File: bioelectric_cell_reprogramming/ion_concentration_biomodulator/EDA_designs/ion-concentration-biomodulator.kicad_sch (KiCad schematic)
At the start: 52 parts, among them J1 532610671, J10 39-53-2045, J11 Conn_01x14_Pin, J12 Conn_01x14_Pin, J13 39-53-2045, J14 39-53-2045, J15 Conn_ARM_SWD_TagConnect_TC2030, J16 IPL1-104-01-L-D-K, J17 Conn_01x02_Pin, J18 EJ508A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

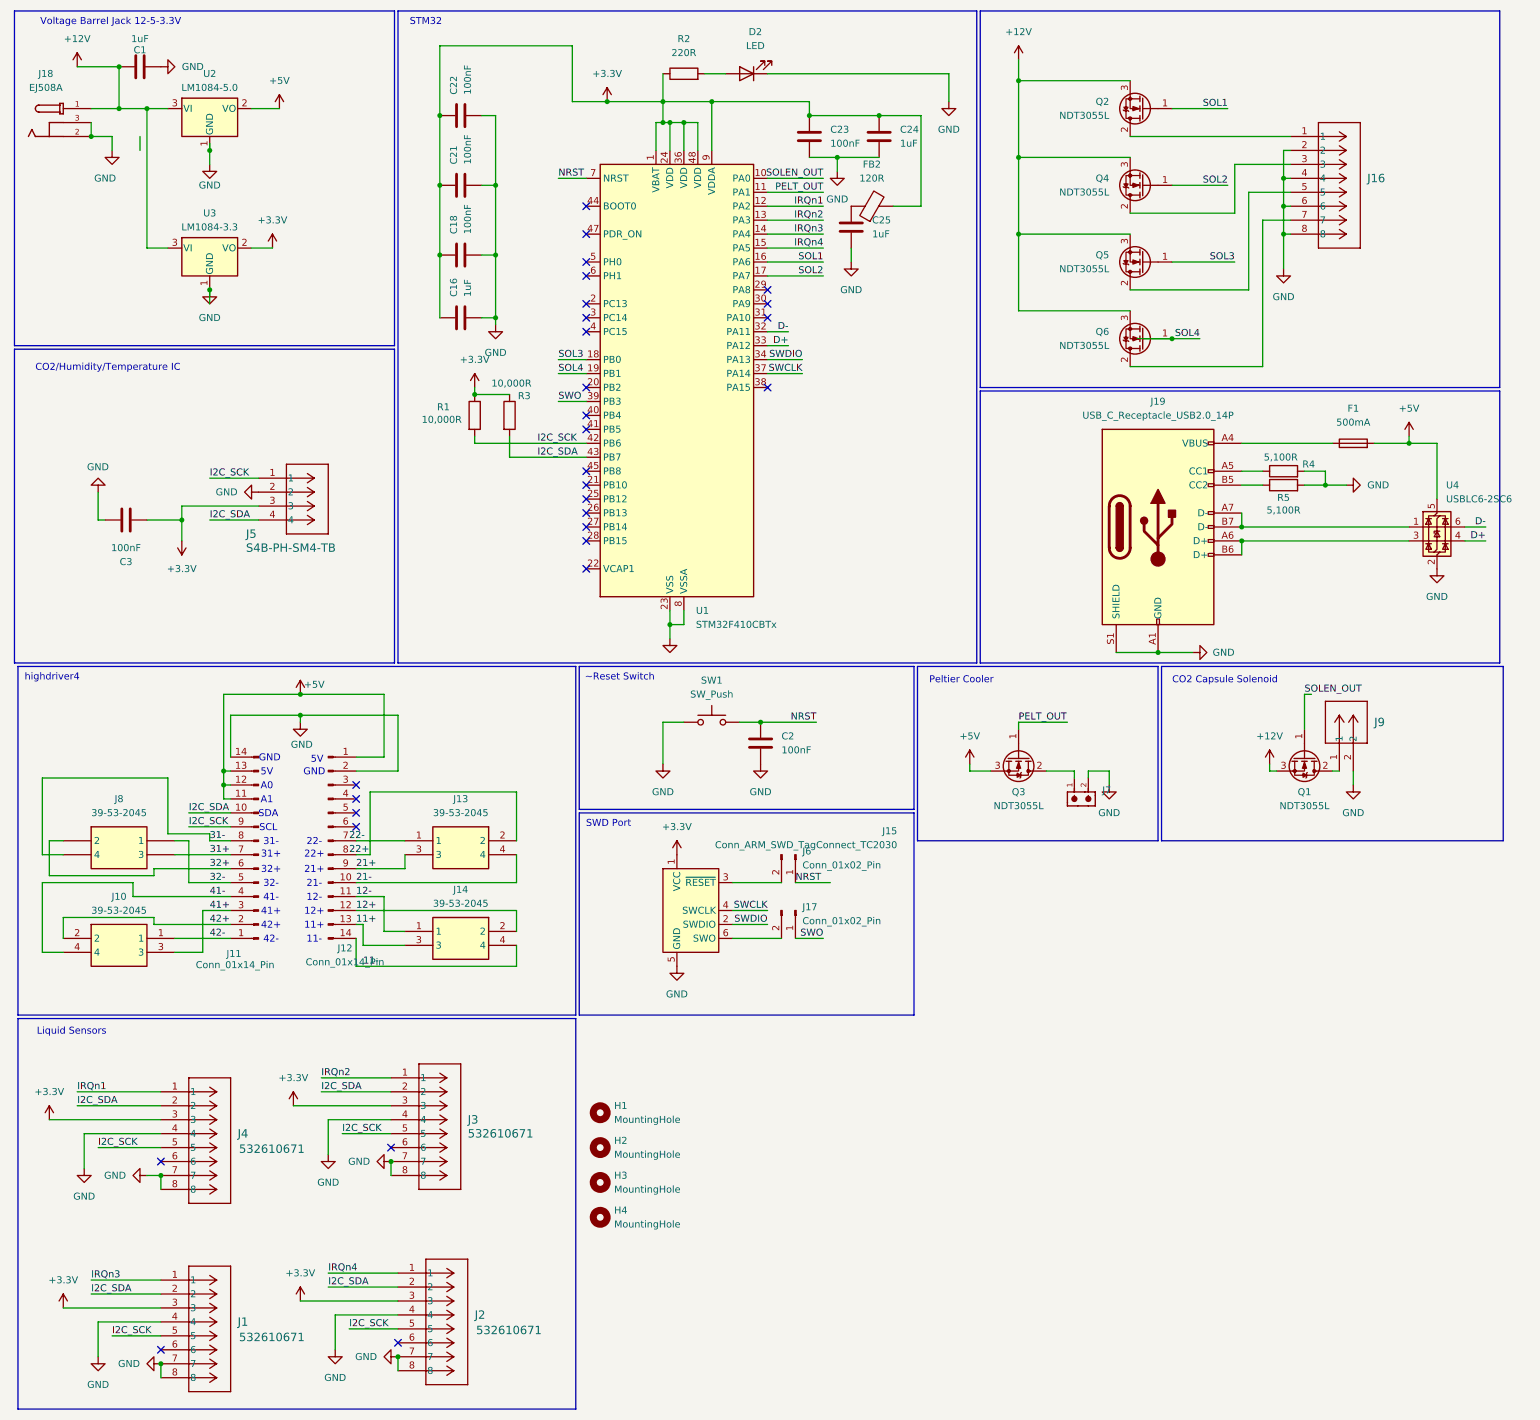
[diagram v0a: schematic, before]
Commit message: Pushed net changes to v7 ICBM
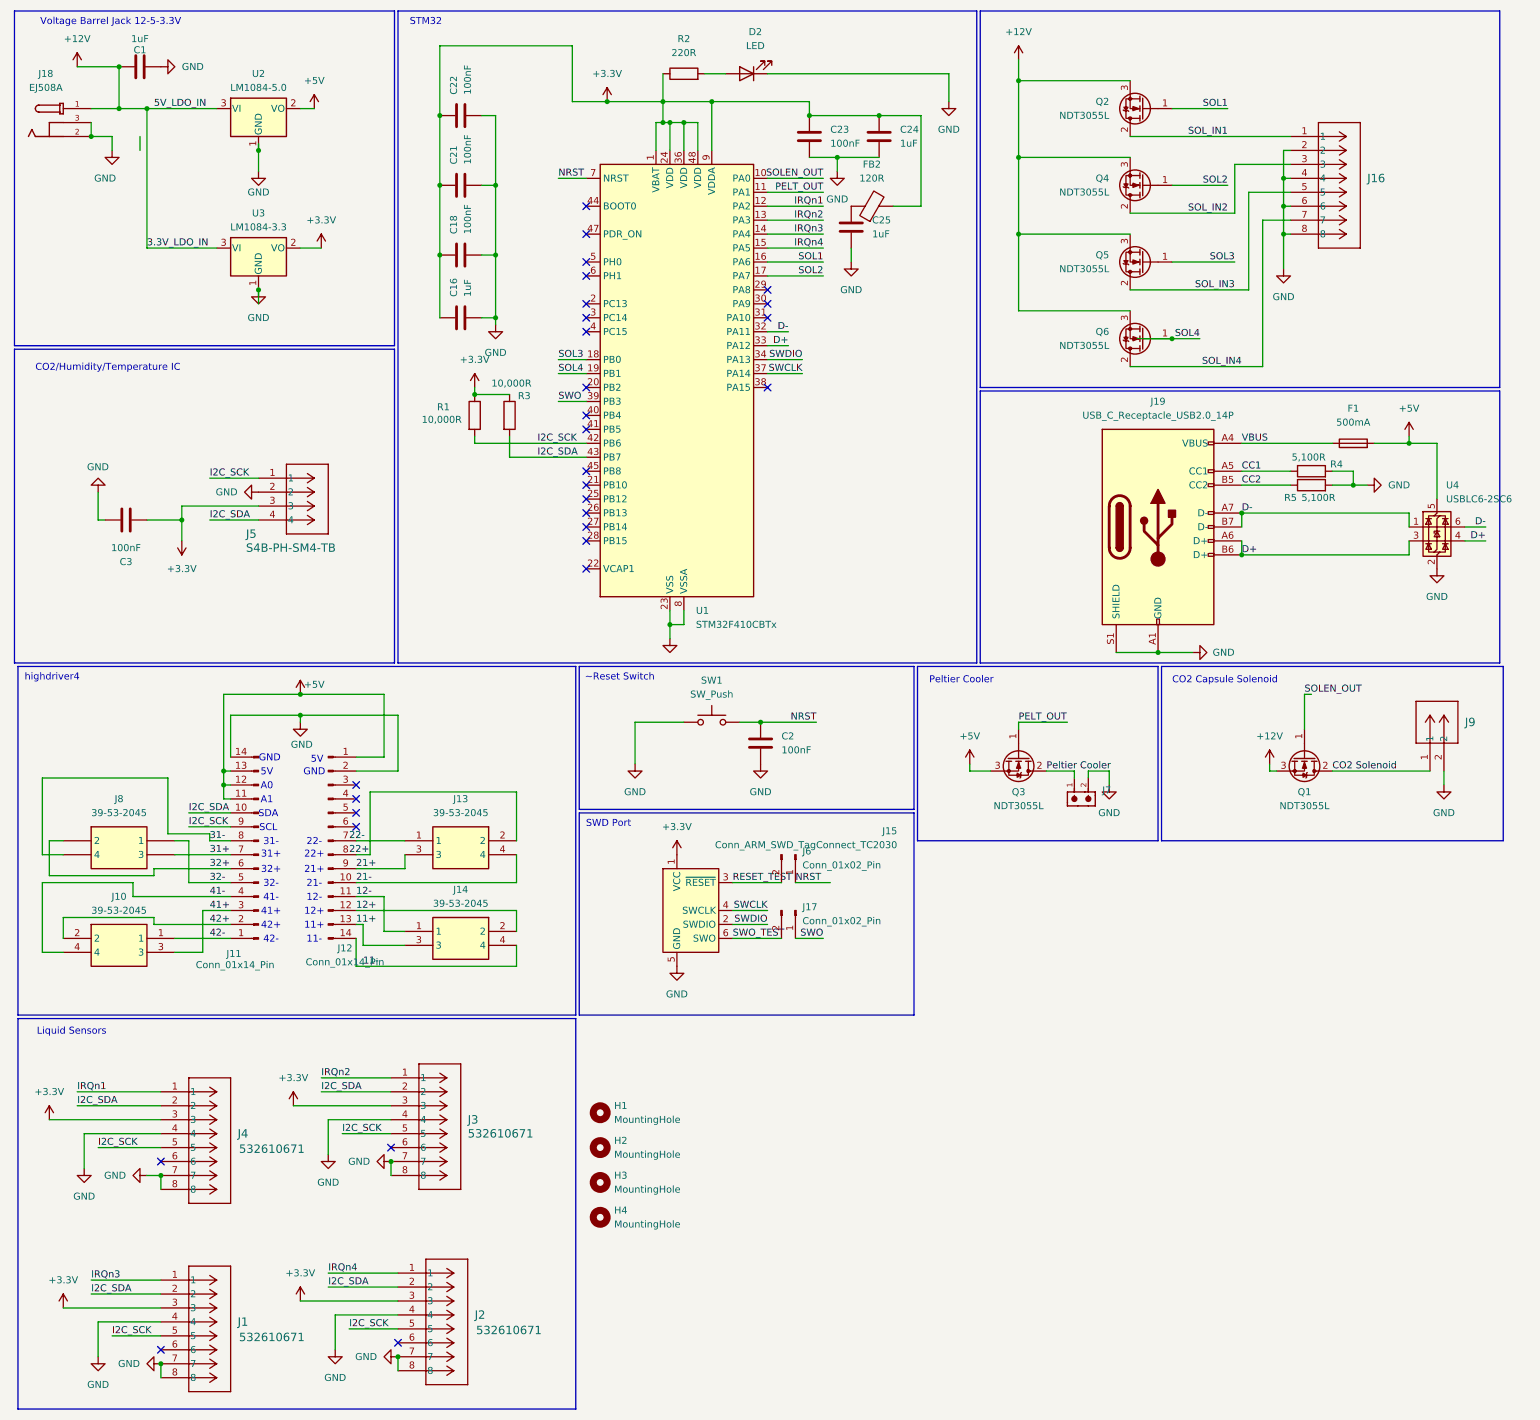
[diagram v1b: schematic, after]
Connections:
- net D+: now also J19.A6 (D+), J19.B6 (D+), U4.3 (I/O2)
- net D-: now also J19.A7 (D-), J19.B7 (D-), U4.1 (I/O1)
- net SOL_IN1: now reaches J16.1, Q2.2 (D)
- net SOL_IN2: now reaches J16.3, Q4.2 (D)
- net SOL_IN3: now reaches J16.5, Q5.2 (D)
- net SOL_IN4: now reaches J16.7, Q6.2 (D)
- net CO2 Solenoid: now reaches J9.1, Q1.2 (D)
- net SWO_TEST: now reaches J15.6 (SWO), J17.2 (Pin_2)
- net VBUS: now reaches F1.1, J19.A4 (VBUS), J19.A9 (VBUS), J19.B4 (VBUS), J19.B9 (VBUS)
- net CC1: now reaches J19.A5 (CC1), R4.1
- net RESET_TEST: now reaches J15.3 (~{RESET}), J6.2 (Pin_2)
- net CC2: now reaches J19.B5 (CC2), R5.1
- net Peltier Cooler: now reaches J7.1, Q3.2 (D)
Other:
- moved on the sheet: J9, R4, R5, U2, U3
